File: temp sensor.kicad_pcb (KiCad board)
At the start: 2 copper layers, 18.3 x 15.2 mm, 30 parts, among them J1 Conn_01x02_Male, J2 Conn_01x04_Male, J3 Conn_01x04_Male, J4 USB_B_Micro, U1 LIS2DE12, U2 TLV62569DBV, U3 BME280, U4 Si7020-A20, U5 SN65220, U6 HDC1080, Y1 Crystal

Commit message: minor update
Signed-off-by: lokimetasmith <lokimail@gmail.com>
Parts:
- added IC1: ESP32-C3-MINI-1, ESP32C3MINI1, F.Cu at (76.7, 47.8)
- moved J4 30.1 mm to (59.9, 84.7)
- moved U1 28.5 mm to (62.5, 82.9)
- moved J2 26.4 mm to (63.8, 83.8)
- moved U6 26.0 mm to (65.8, 50.5), turned to 270 degrees
- moved R9 19.9 mm to (65.1, 67.8)
- moved J3 19.2 mm to (98.6, 54.4)
- moved R13 18.3 mm to (67.7, 74.0)
- moved R10 17.3 mm to (69.0, 74.7)
- moved U5 17.1 mm to (89.7, 51.6), turned to 270 degrees
- moved R4 16.4 mm to (70.3, 75.4)
- moved C9 15.6 mm to (71.6, 76.0)
- moved R12 15.2 mm to (86.1, 52.8), turned to 180 degrees
- moved Y1 14.7 mm to (72.4, 60.5)
- moved C6 11.1 mm to (74.2, 70.5)
- moved C5 10.2 mm to (93.7, 73.3)
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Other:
- board size 18.3 x 15.2 mm -> 19.6 x 15.9 mm

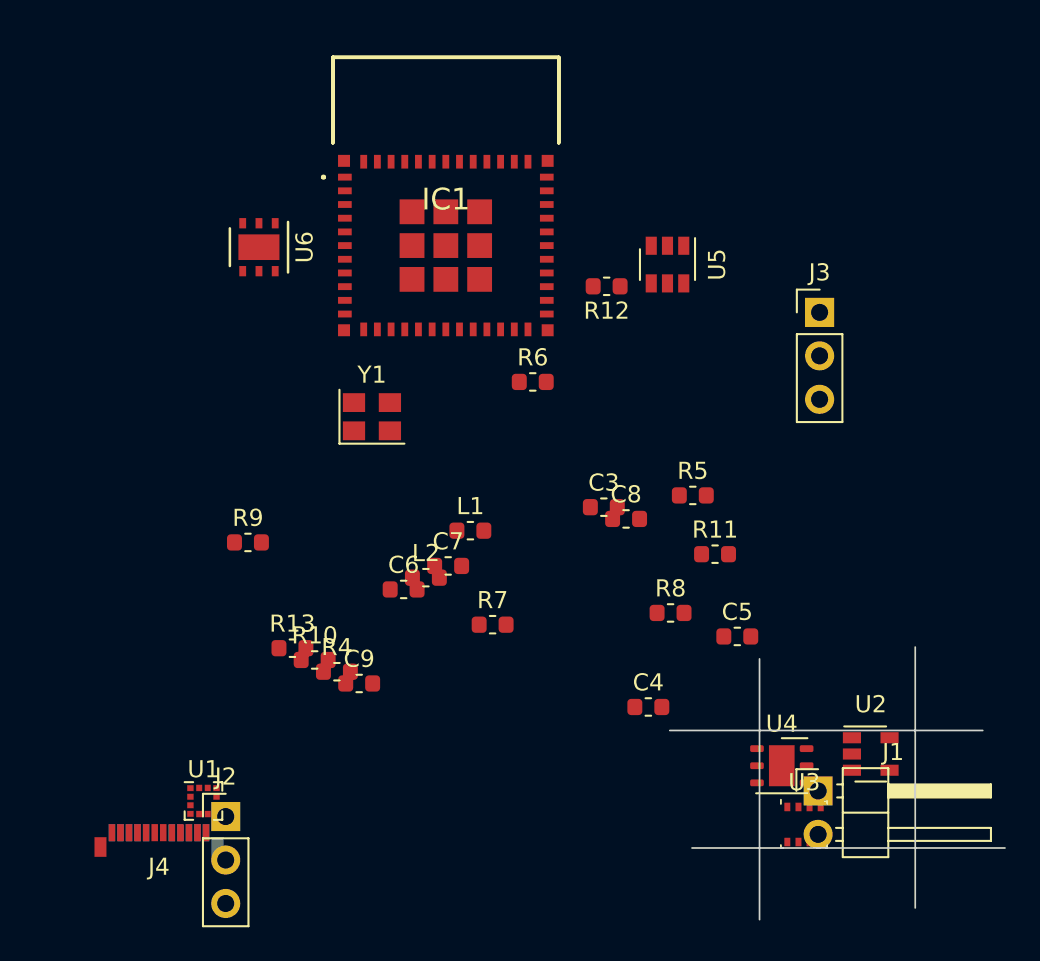
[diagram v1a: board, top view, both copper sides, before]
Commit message: initial layout and silk screen options
Signed-off-by: lokimetasmith <lokimail@gmail.com>
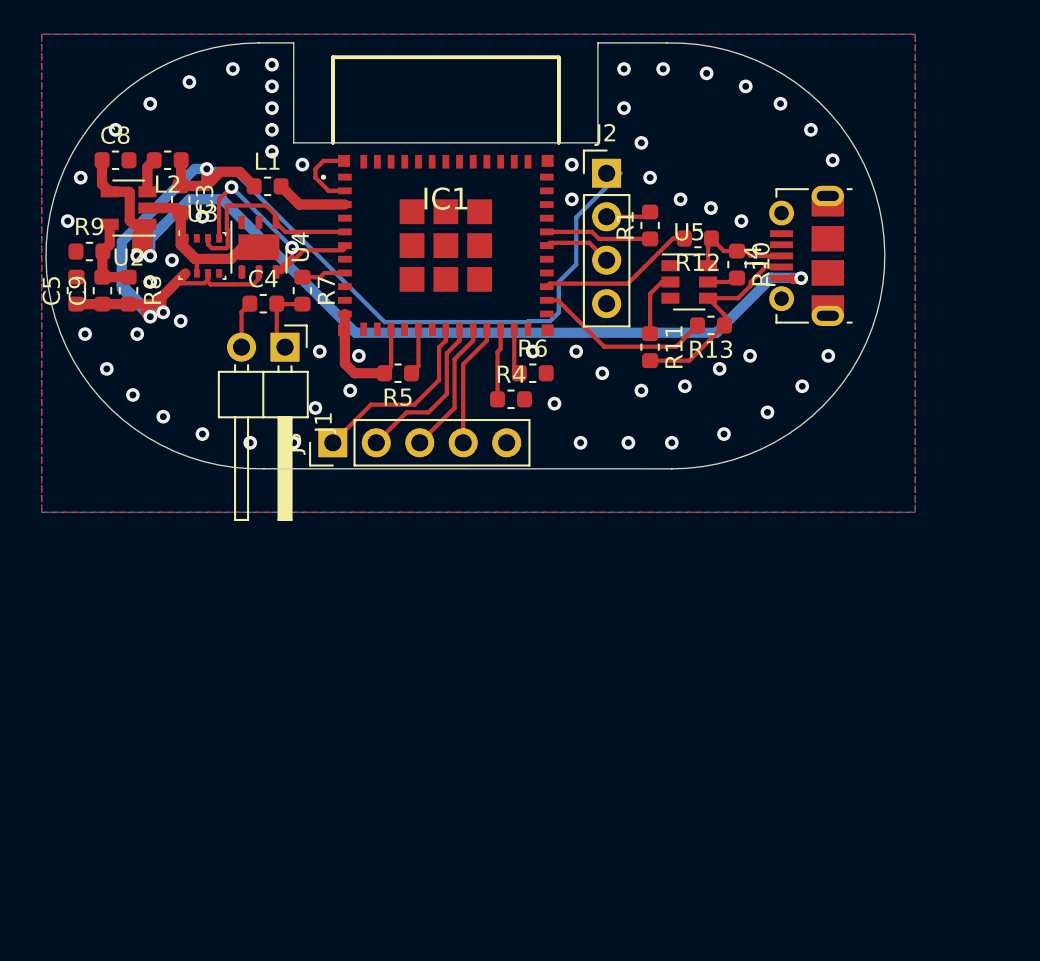
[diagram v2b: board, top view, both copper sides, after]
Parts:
- removed C6, C7: C_Small, Capacitor_SMD:C_0603_1608Metric
- removed U1: LIS2DE12, Package_LGA:LGA-12_2x2mm_P0.5mm
- removed U6: HDC1080, Package_SON:Texas_PWSON-N6
- removed Y1: Crystal, Oscillator:Oscillator_SMD_Abracon_ASE-4Pin_3.2x2.5mm
- added R1: 499R, Resistor_SMD:R_0603_1608Metric, F.Cu at (88.6, 49.3)
- C4: value C_Small -> 1u
- IC1: footprint ESP32C3MINI1 -> ESP32-C3-MINI-1:ESP32C3MINI1
- J2: footprint Connector_PinHeader_2.54mm:PinHeader_1x03_P2.54mm_Vertical -> Connector_PinHeader_2.54mm:PinHeader_1x04_P2.54mm_Vertical
- J3: value Conn_01x04_Male -> Conn_01x05_Male; footprint Connector_PinHeader_2.54mm:PinHeader_1x03_P2.54mm_Vertical -> Connector_PinHeader_2.54mm:PinHeader_1x05_P2.54mm_Vertical
- J4: footprint Connector_USB:USB_C_Plug_Molex_105444 -> Connector_USB:USB_Micro-B_Molex-105017-0001
- moved U2 53.8 mm to (58.2, 48.3), turned to 180 degrees
- moved J4 50.7 mm to (97.8, 51.1), turned to 90 degrees
- moved U3 48.4 mm to (62.5, 51.1)
- moved J2 43.7 mm to (86.1, 46.2)
- moved C5 43.6 mm to (55.1, 53.1), turned to 90 degrees
- moved U4 43.0 mm to (65.8, 50.5), turned to 270 degrees
- moved J1 40.5 mm to (67.3, 56.4), turned to 270 degrees
- moved R8 36.9 mm to (58.2, 53.1), turned to 270 degrees
- moved C8 36.5 mm to (57.4, 45.5)
- moved R10 33.8 mm to (93.7, 51.6), turned to 270 degrees
- moved C4 32.6 mm to (66.0, 53.8)
- moved R13 30.9 mm to (92.2, 55.1), turned to 180 degrees
- moved C3 30.6 mm to (61.2, 47.8), turned to 270 degrees
- moved J3 29.5 mm to (70.1, 62.0), turned to 90 degrees
- moved L2 28.7 mm to (60.5, 45.5), turned to 180 degrees
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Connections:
- IC1 pad 31: /TDX0 -> Net-(IC1-Pad31)
- IC1 pad 5: /SCL -> /SDA
- IC1 pad 6: /SDA -> /SCL
- U5 pad 2: Net-(R10-Pad2) -> Net-(R11-Pad1)
- U5 pad 4: Net-(J4-Pad3) -> Net-(J4-Pad2)
- U5 pad 5: Net-(R11-Pad1) -> Net-(R10-Pad2)
- U5 pad 6: Net-(J4-Pad2) -> Net-(J4-Pad3)
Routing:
- net +3V3: track 0.00 -> 72.5 mm, vias 0 -> 3
- net +5V: track 0.00 -> 58.2 mm, vias 0 -> 3
- net GND: track 0.00 -> 28.4 mm, vias 0 -> 58
- net /SCL: track 0.00 -> 14.9 mm, vias 0 -> 2
- net Net-(J4-Pad2): track 0.00 -> 12.4 mm
- net /SDA: track 0.00 -> 11.8 mm
- net /TMS: track 0.00 -> 10.8 mm
- net /USB_D-: track 0.00 -> 10.4 mm
- net /TDI: track 0.00 -> 9.38 mm
- net /USB_D+: track 0.00 -> 9.21 mm
- net /TCK: track 0.00 -> 7.92 mm
- net /TDO: track 0.00 -> 7.20 mm
- net Net-(IC1-Pad31): track 0.00 -> 6.21 mm
- net Net-(J4-Pad3): track 0.00 -> 6.19 mm
- net Net-(C9-Pad2): track 0.00 -> 4.79 mm
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- added copper zone on B.Cu, net GND
- added copper zone on F.Cu, net GND
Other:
- board size 19.6 x 15.9 mm -> 49 x 24.9 mm

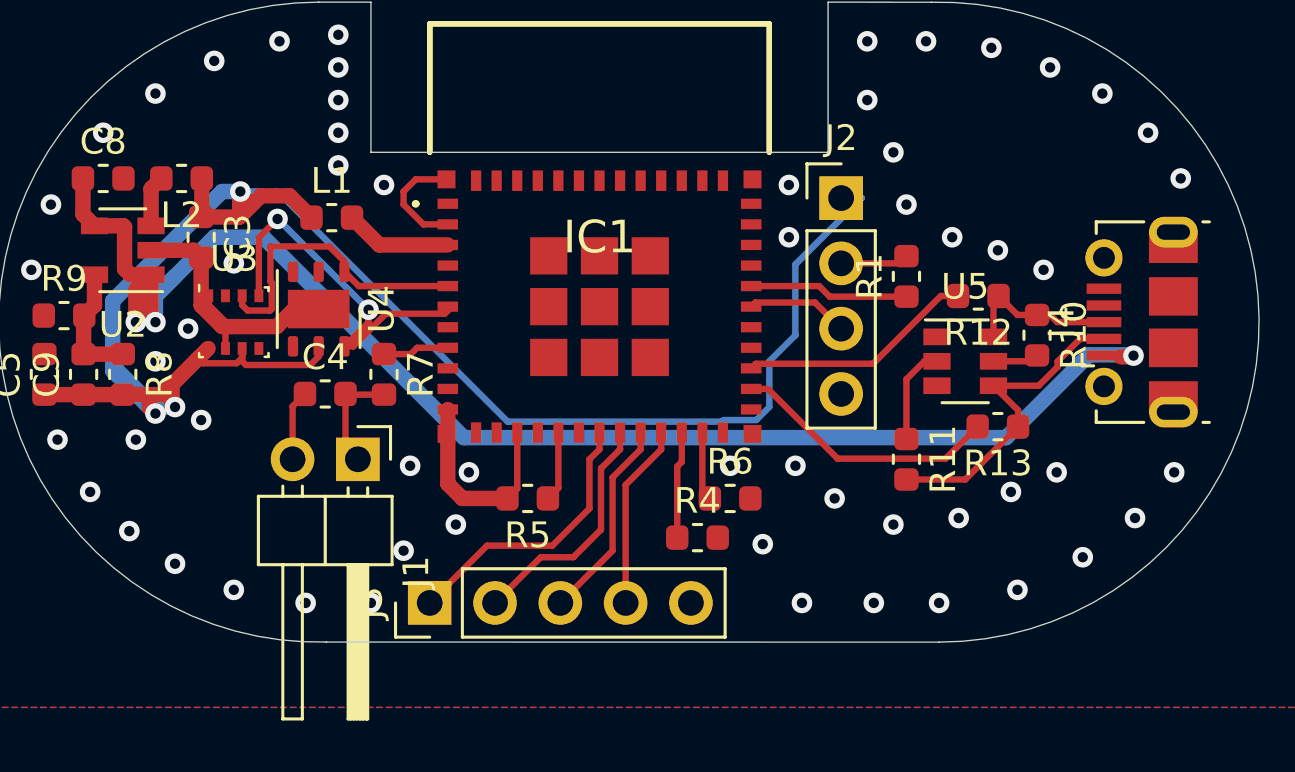
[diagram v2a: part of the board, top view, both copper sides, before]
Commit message: minor layout update and pic of humidity sensor cover concept
Signed-off-by: lokimetasmith <lokimail@gmail.com>
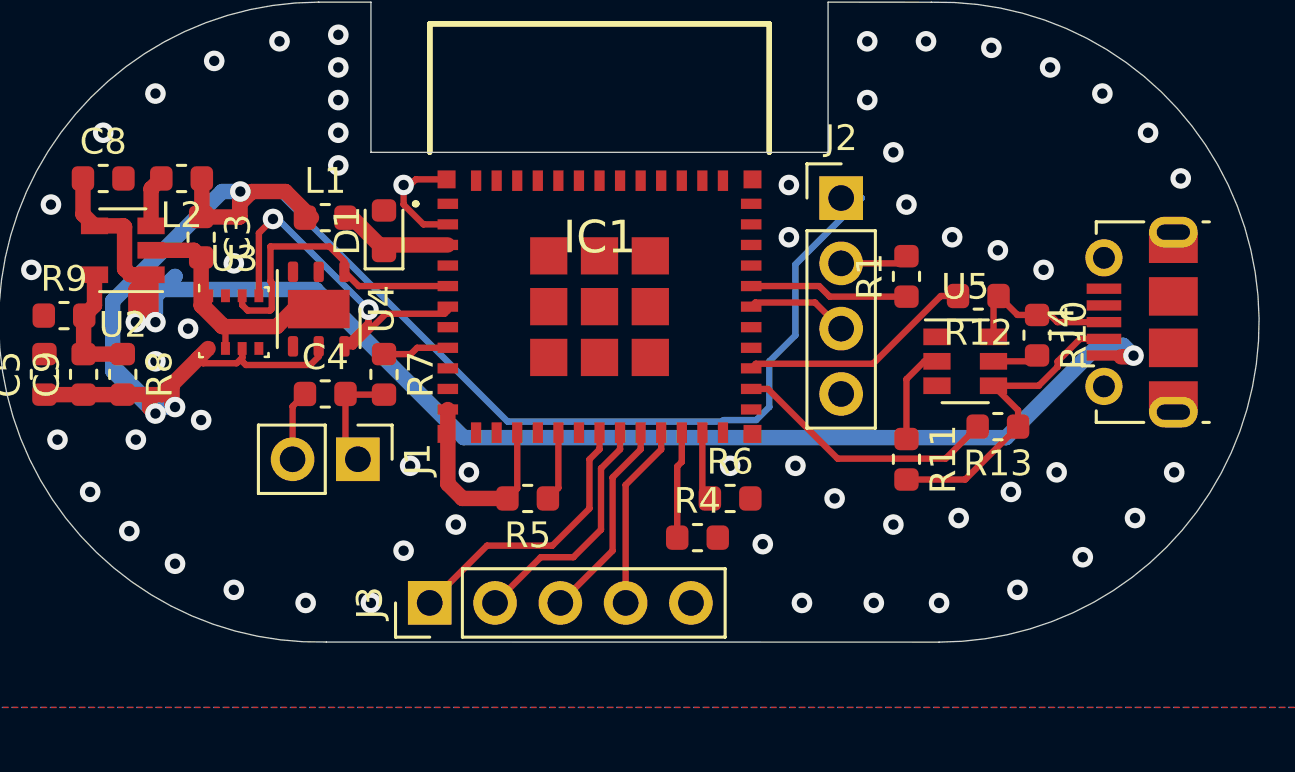
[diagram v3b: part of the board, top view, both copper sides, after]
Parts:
- added D1: D_TVS, Diode_SMD:D_0603_1608Metric, F.Cu at (68.3, 47.5)
- J1: footprint Connector_PinHeader_2.54mm:PinHeader_1x02_P2.54mm_Horizontal -> Connector_PinHeader_2.54mm:PinHeader_1x02_P2.54mm_Vertical
- moved L1 0.25 mm to (66.0, 47.0)
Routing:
- net +5V: track 58.2 -> 56.8 mm

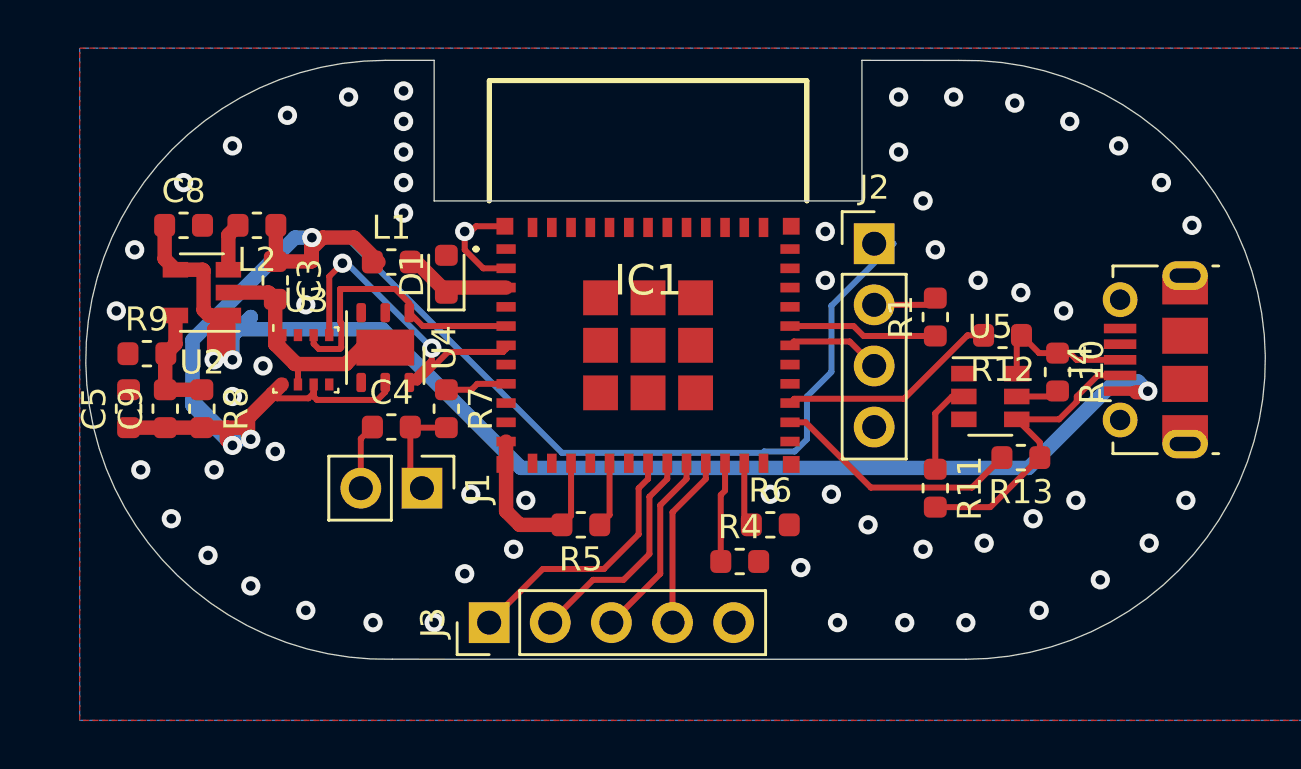
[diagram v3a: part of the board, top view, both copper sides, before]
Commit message: layout and part changes
Signed-off-by: lokimetasmith <lokimail@gmail.com>
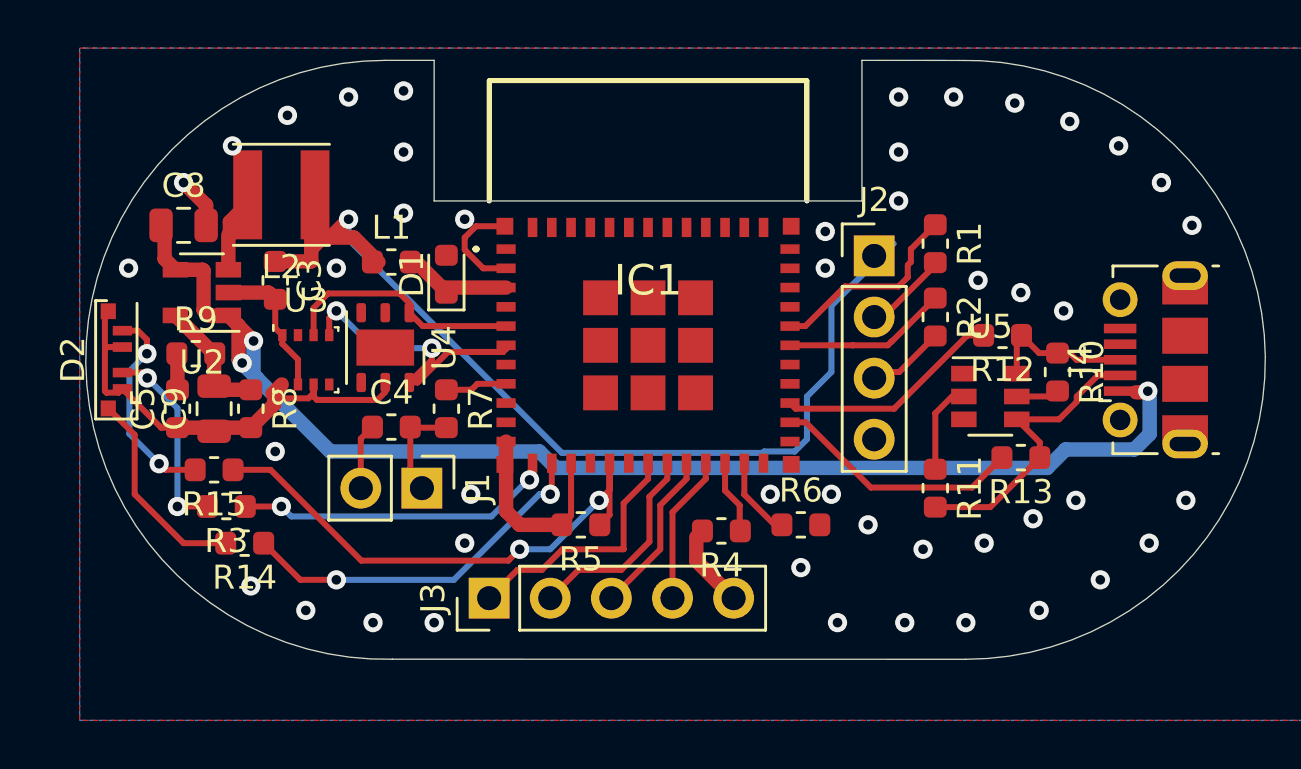
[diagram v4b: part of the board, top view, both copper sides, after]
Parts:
- added D2: LED_RGB, LED_SMD:LED_Cree-PLCC6_4.7x1.5mm, F.Cu at (54.6, 51.1)
- added R14: 10K, Resistor_SMD:R_0603_1608Metric, F.Cu at (59.9, 58.7)
- added R15: 10K, Resistor_SMD:R_0603_1608Metric, F.Cu at (58.7, 55.6)
- added R2: 499R, Resistor_SMD:R_0603_1608Metric, F.Cu at (88.6, 49.3)
- added R3: 10K, Resistor_SMD:R_0603_1608Metric, F.Cu at (59.2, 57.1)
- C8: value C_Small -> 4.7u; footprint Capacitor_SMD:C_0603_1608Metric -> Capacitor_SMD:C_0805_2012Metric
- C9: value C_Small -> 10u; footprint Capacitor_SMD:C_0603_1608Metric -> Capacitor_SMD:C_0805_2012Metric
- L2: footprint Inductor_SMD:L_0603_1608Metric -> Inductor_SMD:L_Taiyo-Yuden_MD-4040
- R8: value 10K -> 470k
- R9: value 10K -> 120K
- moved R1 3.05 mm to (88.6, 46.2), turned to 270 degrees
- moved R8 2.03 mm to (60.2, 53.1)
- moved C5 2.03 mm to (57.1, 53.1)
- moved C9 2.03 mm to (58.7, 53.1)
- moved R9 2.03 mm to (57.9, 50.8)
- moved L2 1.63 mm to (61.5, 44.2)
- moved R4 1.48 mm to (79.8, 58.2), turned to 180 degrees
- moved R6 1.27 mm to (83.1, 57.9)
- moved J3 1.02 mm to (70.1, 61.0)
- moved J2 0.51 mm to (86.1, 46.7)
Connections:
- net Net-(IC1-Pad16) renamed /io10
- IC1 pad 30: /RTX0 -> Net-(IC1-Pad30)
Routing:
- net /io10: track 2.73 -> 22.3 mm, vias 0 -> 2
- net /io1: track 0.00 -> 15.3 mm, vias 0 -> 2
- net /io0: track 0.00 -> 13.3 mm, vias 0 -> 2
- net +3V3: track 72.9 -> 63.0 mm, vias 3 -> 1
- net Net-(D2-Pad2): track 0.00 -> 8.75 mm, vias 0 -> 2
- net Net-(D2-Pad6): track 0.00 -> 8.65 mm
- net Net-(D2-Pad4): track 0.00 -> 8.23 mm, vias 0 -> 2
- net Net-(IC1-Pad30): track 0.00 -> 6.85 mm
- net +5V: track 56.8 -> 53.1 mm
- net /SCL: track 15.0 -> 12.3 mm
- net Net-(IC1-Pad31): track 6.21 -> 8.39 mm
- net /SDA: track 11.8 -> 10.2 mm
- net Net-(L2-Pad2): track 2.01 -> 3.42 mm
- net /TCK: track 7.92 -> 6.90 mm
- net /TDO: track 7.20 -> 6.18 mm
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
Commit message: Signed-off-by: lokimetasmith <lokimail@gmail.com>
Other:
- outline, holes or cut-outs redrawn

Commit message: bom and pcb changes, need to add a switch still.
Signed-off-by: lokimetasmith <lokimail@gmail.com>
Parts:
- removed J1: Conn_01x02_Male, Connector_PinHeader_2.54mm:PinHeader_1x02_P2.54mm_Vertical
- added C1: 0.1u, Capacitor_SMD:C_0603_1608Metric, F.Cu at (64.9, 54.1)
- added R16: 10K, Resistor_SMD:R_0603_1608Metric, F.Cu at (64.9, 45.6)
- added R17: 10K, Resistor_SMD:R_0603_1608Metric, F.Cu at (66.4, 45.6)
- added U1: SHTC3, Sensor_Humidity:Sensirion_DFN-4-1EP_2x2mm_P1mm_EP0.7x1.6mm, F.Cu at (68.3, 49.7)
- D1: value D_TVS -> 3.3v_TVS
- R14, R15: value 10K -> 100
- R3: value 10K -> 200
- moved C8 39.6 mm to (95.5, 56.3)
- moved U2 37.1 mm to (93.6, 59.2), turned to 0 degrees
- moved L2 32.1 mm to (89.4, 60.1), turned to 0 degrees
- moved C9 27.9 mm to (86.1, 58.4)
- moved R9 26.4 mm to (83.1, 58.9), turned to 270 degrees
- moved R8 25.0 mm to (83.8, 61.2), turned to 0 degrees
- moved C5 11.1 mm to (63.4, 43.9)
- moved R3 10.9 mm to (56.5, 46.6)
- moved R14 10.3 mm to (56.8, 48.9), turned to 270 degrees
- moved R2 4.95 mm to (91.9, 45.6), turned to 0 degrees
- moved R13 4.32 mm to (87.9, 55.1)
- moved J2 4.21 mm to (88.1, 43.0), turned to 90 degrees
- moved R15 4.15 mm to (56.8, 51.9), turned to 90 degrees
- moved U4 3.64 mm to (62.2, 49.8)
- moved R12 3.57 mm to (87.9, 49.8)
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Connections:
- net Net-(J4-Pad2) renamed /D-
- net Net-(J4-Pad3) renamed /D+
- C9 pad 2: Net-(C9-Pad2) -> GND
- D2 pad 1: +3V3 -> Net-(D2-Pad1)
- D2 pad 3: +3V3 -> Net-(D2-Pad3)
- D2 pad 4: Net-(D2-Pad4) -> +3V3
- D2 pad 6: Net-(D2-Pad6) -> +3V3
- R10 pad 2: Net-(R10-Pad2) -> GND
- R11 pad 1: Net-(R11-Pad1) -> GND
- R14 pad 2: Net-(D2-Pad6) -> Net-(D2-Pad2)
- R15 pad 2: Net-(D2-Pad2) -> Net-(D2-Pad3)
- R3 pad 2: Net-(D2-Pad4) -> Net-(D2-Pad1)
- R8 pad 1: Net-(C9-Pad2) -> Net-(R8-Pad1)
- R9 pad 2: Net-(C9-Pad2) -> Net-(R8-Pad1)
- U2 pad 5: Net-(C9-Pad2) -> Net-(R8-Pad1)
- U3 pad 2: Net-(U3-Pad2) -> +3V3
- U3 pad 5: Net-(U3-Pad5) -> GND
- U5 pad 2: Net-(R11-Pad1) -> GND
- U5 pad 5: Net-(R10-Pad2) -> GND
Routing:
- net +3V3: track 63.0 -> 103.6 mm, vias 1 -> 5
- net +5V: track 53.1 -> 17.4 mm, vias 3 -> 0
- net Net-(R8-Pad1): track 0.00 -> 22.1 mm, vias 0 -> 2
- net GND: track 28.2 -> 44.8 mm, vias 46 -> 18
- net /io0: track 13.3 -> 25.2 mm
- net /io1: track 15.3 -> 24.4 mm
- net Net-(D2-Pad6): track 8.65 -> 0.00 mm
- net Net-(D2-Pad4): track 8.23 -> 0.00 mm, vias 2 -> 0
- net Net-(D2-Pad2): track 8.75 -> 1.95 mm, vias 2 -> 0
- net /io10: track 22.3 -> 28.8 mm
- net Net-(C9-Pad2): track 5.33 -> 0.00 mm
- net /SCL: track 12.3 -> 17.1 mm, vias 2 -> 3
- net /USB_D-: track 10.4 -> 5.80 mm
- net /D+: track 6.19 -> 10.0 mm
- net Net-(R11-Pad1): track 3.80 -> 0.00 mm
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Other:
- board size 49 x 24.9 mm -> 48.2 x 24.9 mm
